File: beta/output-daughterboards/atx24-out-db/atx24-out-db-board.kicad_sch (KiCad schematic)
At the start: 12 parts, among them J1 ATX24 OUT FIELD, J10 TE 63951-1, J11 TE 63951-1, J12 TE 63951-1, J13 TE 63951-1, J14 TE 63951-1, J15 TE 63951-1, J16 TE 63951-1, J17 TE 63951-1, J18 TE 63951-1, J19 TE 63951-1, J20 SIGNAL STUB (1x4 blind-mate)

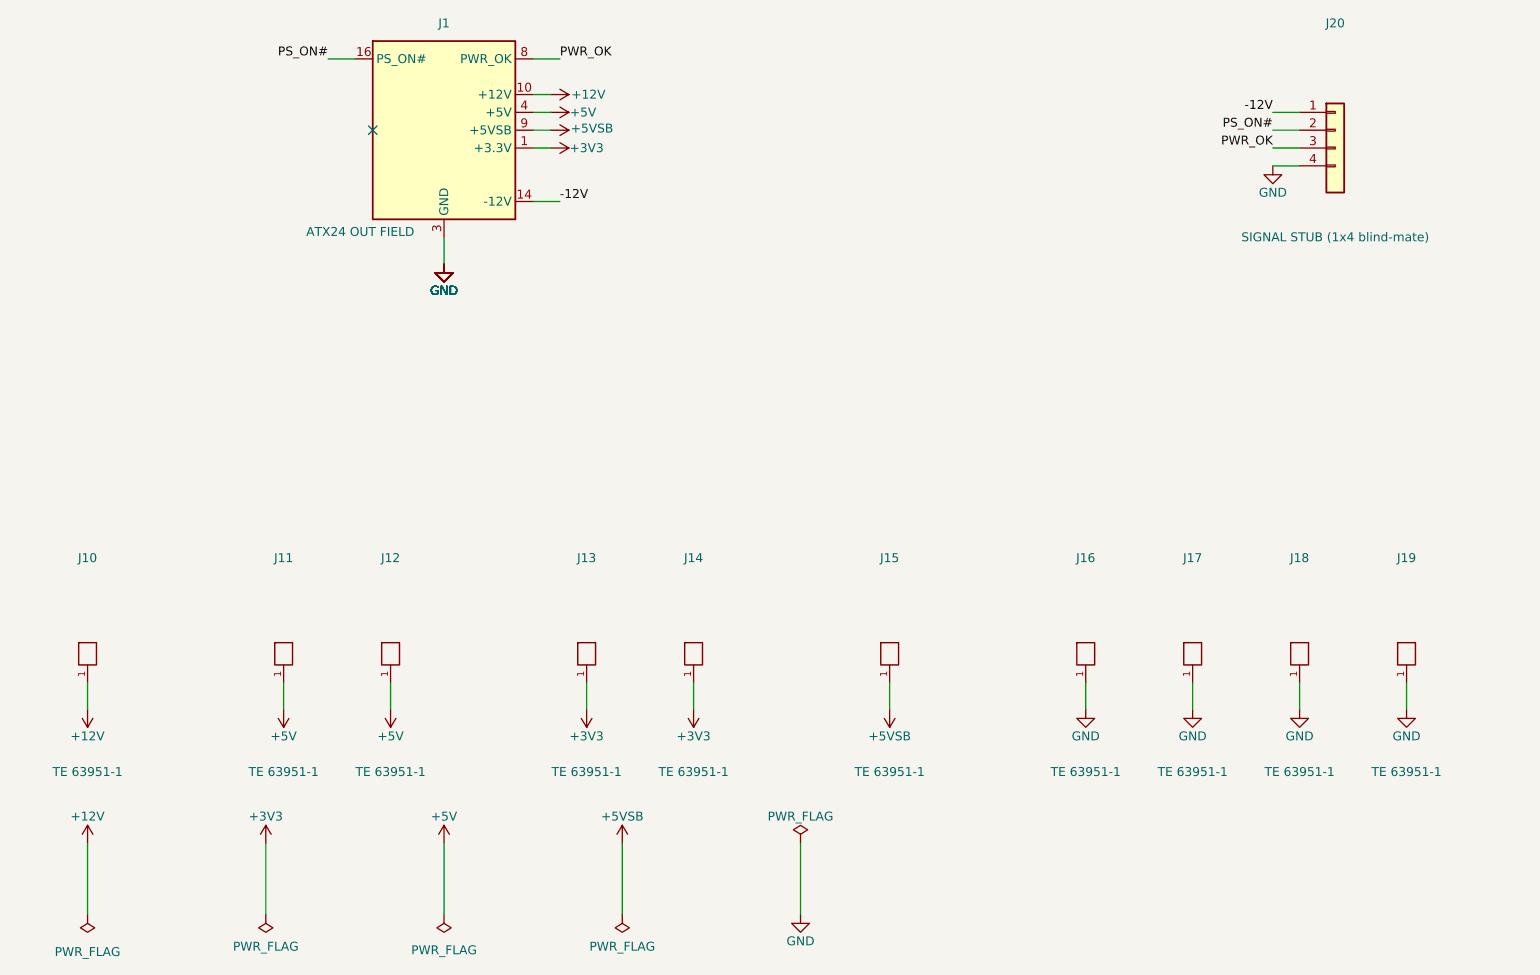
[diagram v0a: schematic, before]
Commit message: Finalize compact Hub and ATX power-layout audit
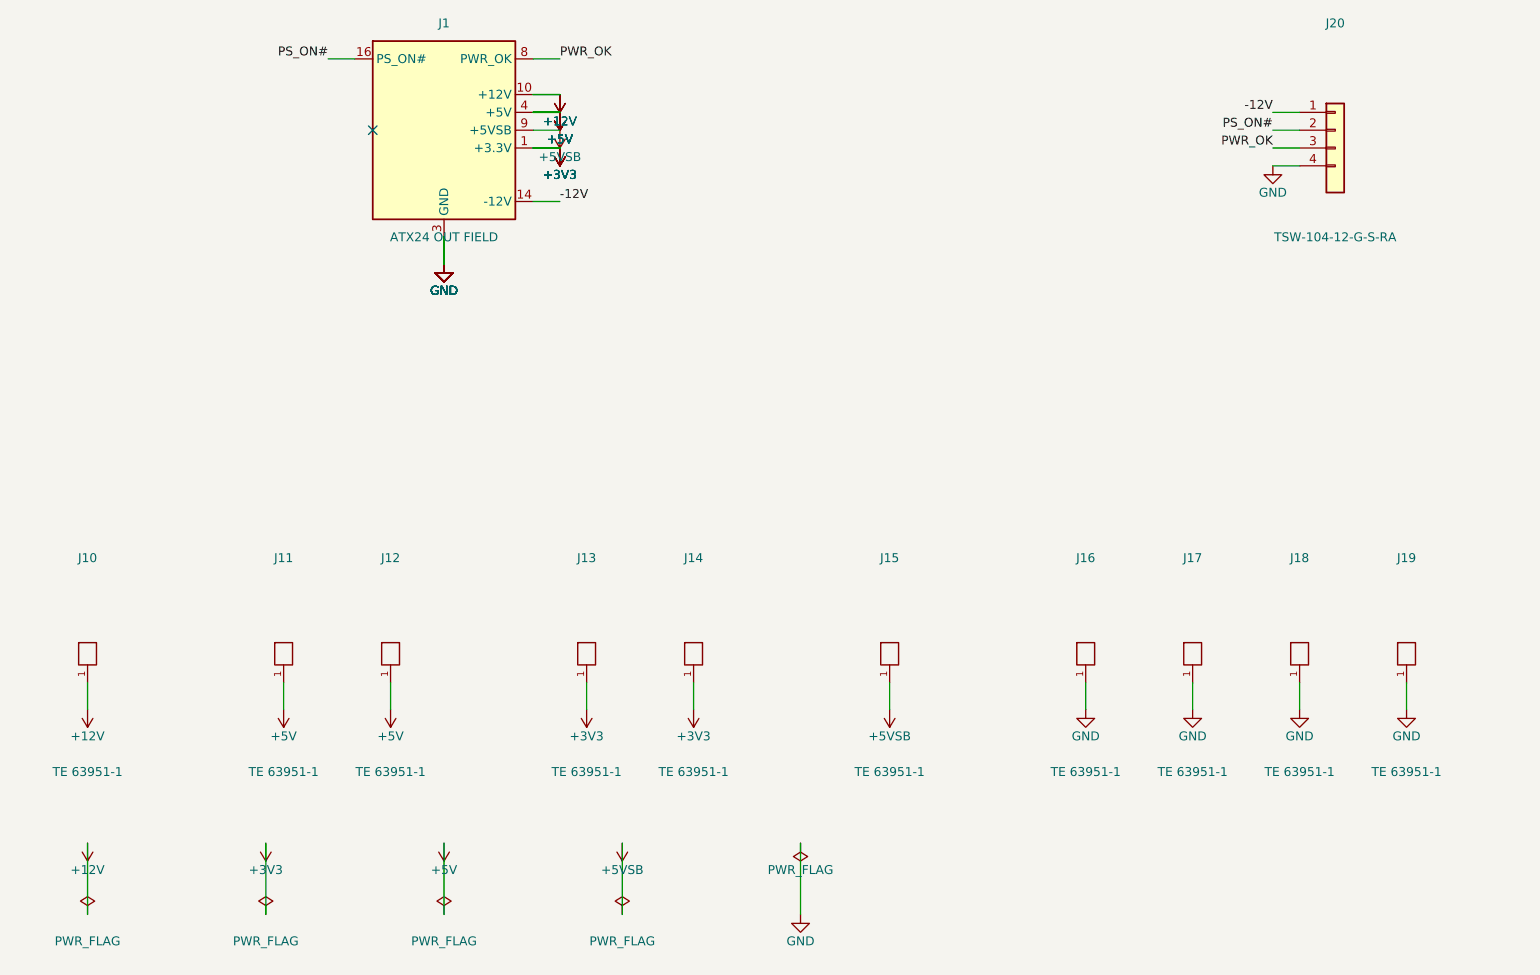
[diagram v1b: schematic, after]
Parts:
- J20: value SIGNAL STUB (1x4 blind-mate) -> TSW-104-12-G-S-RA; MPN (none) -> TSW-104-12-G-S-RA; Manufacturer generic -> Samtec

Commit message: pipeline: integrate route-aware physical design flow
Generalize critical-first placement and routing, future-congestion and power-authority planning, route provenance, process watchdogs, fab/thermal validation, dashboard review, and XFCN integration. Add the supporting board contracts, component libraries, documentation, and regression coverage.
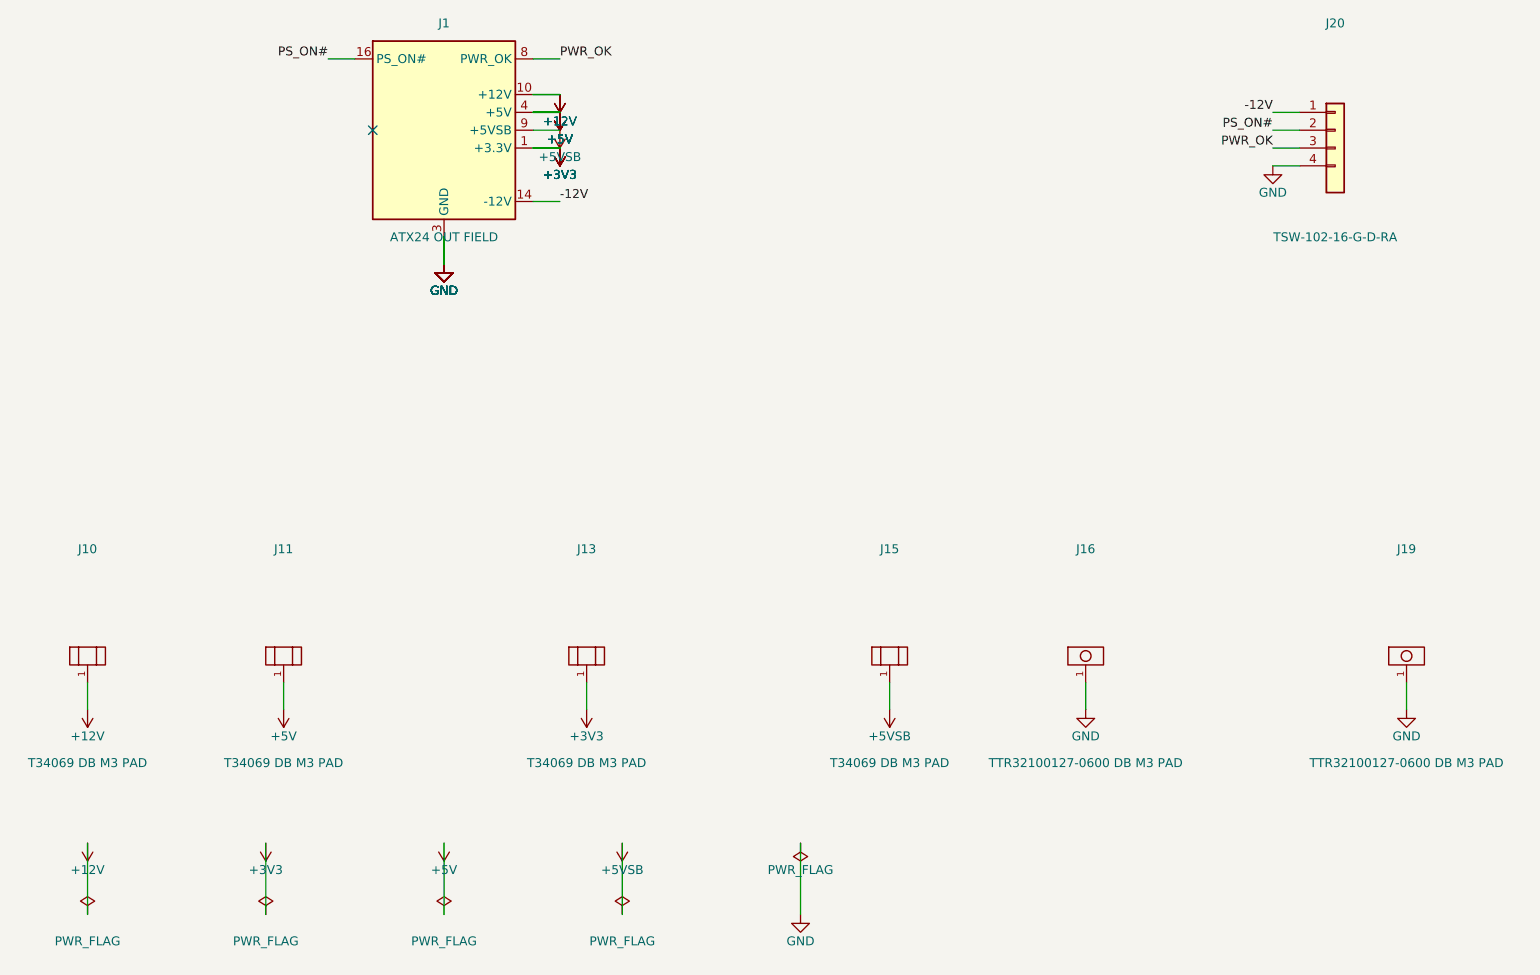
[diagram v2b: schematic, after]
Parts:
- removed J12, J14, J17, J18: TE 63951-1, cec-Connector_Blade:TE_63951-1_FASTON_Tab_250x032_RA_THT, symbol cec-vendor:TE_63951-1_FASTON_Tab
- J10, J11, J13, J15: value TE 63951-1 -> T34069 DB M3 PAD; footprint cec-Connector_Blade:TE_63951-1_FASTON_Tab_250x032_RA_THT -> cec-Connector_Screw:XFCN_T34069_Daughterboard_BoltPad_M3_PROVISIONAL; symbol cec-vendor:TE_63951-1_FASTON_Tab -> cec-Connector_Screw:XFCN_T34069_DB_BoltPad; Integration Note (none) -> Prototype XFCN interface; TE blade architecture remains the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; LCSC C591344 -> (none); MPN 63951-1 -> (none); Manufacturer TE Connectivity -> (none); Source Drawing (none) -> lib/datasheets/XFCN_T34069_C481452.pdf; now left out of the parts list
- J16, J19: value TE 63951-1 -> TTR32100127-0600 DB M3 PAD; footprint cec-Connector_Blade:TE_63951-1_FASTON_Tab_250x032_RA_THT -> cec-Connector_Screw:XFCN_TTR32100127-0600_Daughterboard_BoltPad_M3_PROVISIONAL; symbol cec-vendor:TE_63951-1_FASTON_Tab -> cec-Connector_Screw:XFCN_TTR32100127-0600_DB_BoltPad; Integration Note (none) -> Prototype XFCN interface; TE blade architecture remains the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; LCSC C591344 -> (none); MPN 63951-1 -> (none); Manufacturer TE Connectivity -> (none); Source Drawing (none) -> lib/datasheets/XFCN_TTR32100127-0600_C45384691.pdf; now left out of the parts list
- J20: value TSW-104-12-G-S-RA -> TSW-102-16-G-D-RA; footprint cec-Connector_PinHeader_2.54mm:PinHeader_1x04_P2.54mm_Horizontal_LongPin -> cec-Connector_PinHeader_2.54mm:Samtec_TSW-102-16-G-D-RA_2x02_P2.54mm_Horizontal; MPN TSW-104-12-G-S-RA -> TSW-102-16-G-D-RA; Note (none) -> Mates SSQ-102-03-G-D; 1=-12V, 2=PS_ON#, 3=PWR_OK, 4=GND. Fi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
